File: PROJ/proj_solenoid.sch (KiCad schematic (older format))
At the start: 19 parts

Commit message: creating kicad project for PROJ
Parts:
- removed D?: RED_LED, symbol Device:LED
- removed D?: GREEN_LED, symbol Device:LED
- removed M?: Stepper_Motor_bipolar, symbol Motor:Stepper_Motor_bipolar
- removed R3, R4: 470, symbol Device:R
- removed SW? (x2): SW_Push, symbol Switch:SW_Push
- removed U?: L298HN, Package_TO_SOT_THT:TO-220-15_P2.54x2.54mm_StaggerOdd_Lead4.58mm_Vertical, symbol Driver_Motor:L298HN
- added D?: LED, symbol Device:LED
- added R?: 10k, symbol Device:R
- added SW?: SW_Reed, symbol Switch:SW_Reed
- added U?: 74HC595, symbol My_lib:74HC596
- added U?: analog_keypad, symbol My_lib:analog_keypad
- added U?: 74LS151, symbol 74xx:74LS151
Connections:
- net labels added: Keypad, Magnet_Mux, Magnet_Sensor, Mux_S0, Mux_S1, Mux_S2, Solenoid_CLK, Solenoid_DATA, Solenoid_RESET, Solenoid_STORE
- net labels removed: +12V, Button_User_1, Button_User_2, Green_LED, Motor_IN1, Motor_IN2, Motor_IN3, Motor_IN4, Red_LED
- wire segments 76 -> 82
- no-connect marks 5 -> 9
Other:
- note added: "Each partition will have its own magnet detector, \nwhich will detect if its open or not."
- note added: "Led signaling that partition is open"
- note added: "Multiplexer for connecting multiple sensors"
- note added: "Shift register used for operating solenoids"
- note added: "Solenoid used for locking individual partitions. \nOperated trough shift register."
- note removed: "External psu needed"
- note removed: "LED for potencial notifying user"
- note removed: "Solenoid can be used for locking mechanism.\nMultiple solenoids can be added using shift register."
- note removed: "Stepper motor could be used for mechanism which would allow circular\nmovement of pill partitions, allowing only one to be accest at a time.\nNot big fan of this approach."
- note removed: "Two user buttons \nOne can be used for canceling alarm\nSecond for entering time setup phase\n"
- moved on the sheet: R1, R2, R5

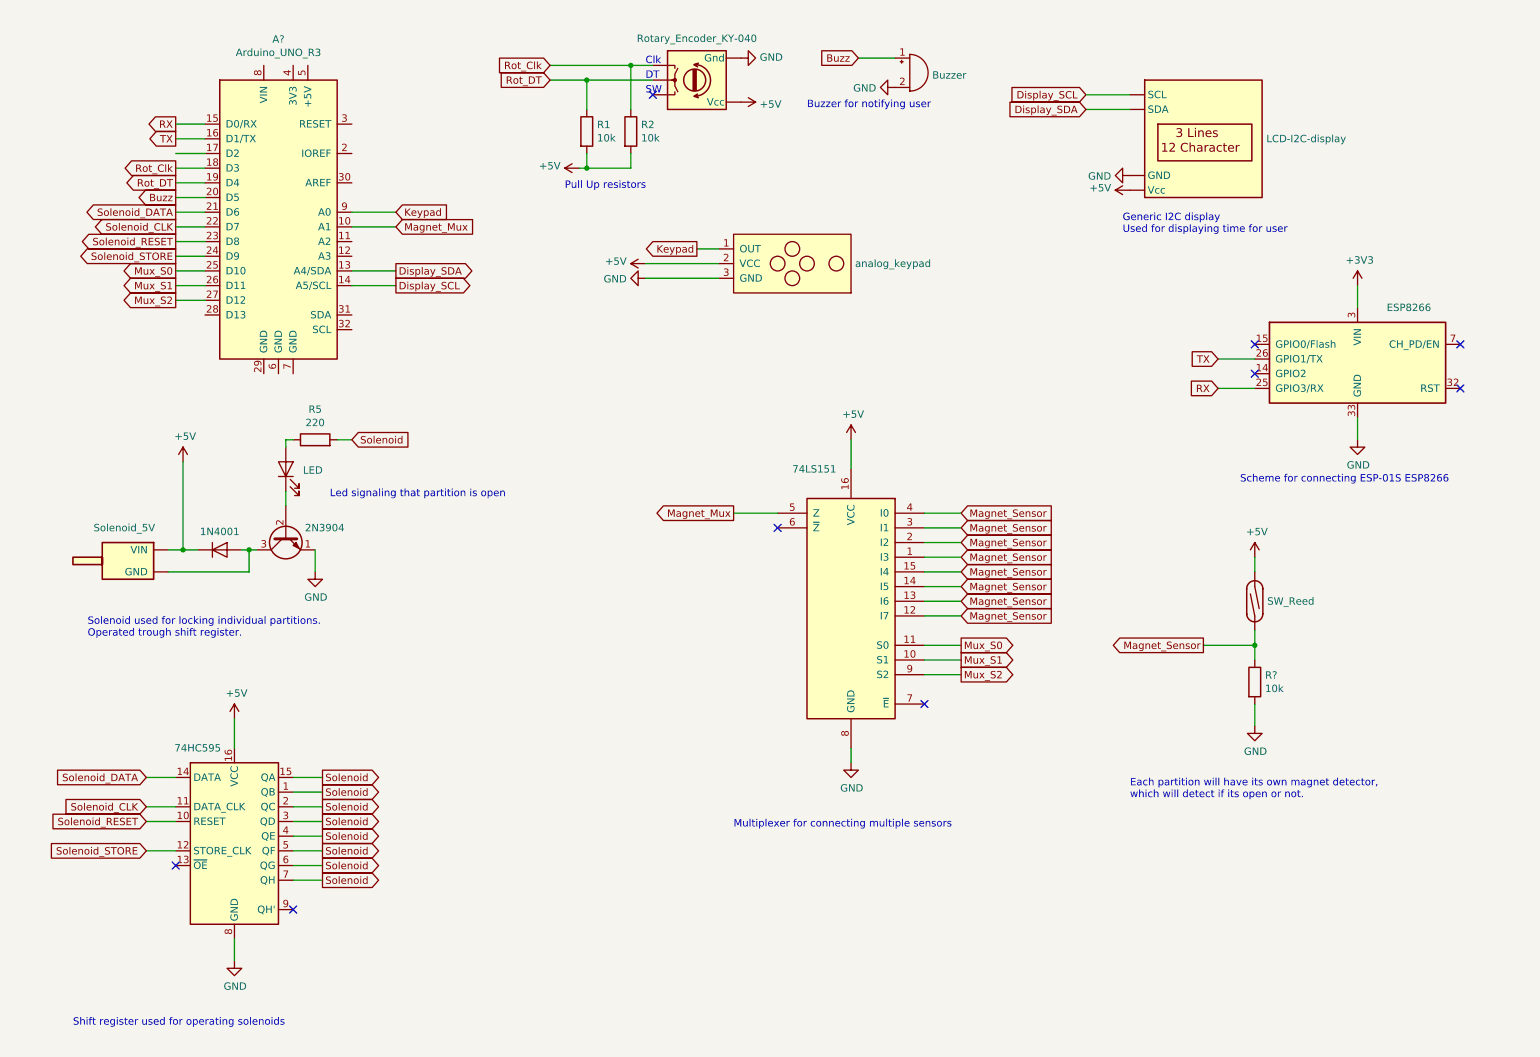
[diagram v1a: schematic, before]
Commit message: adding backup batery to proj
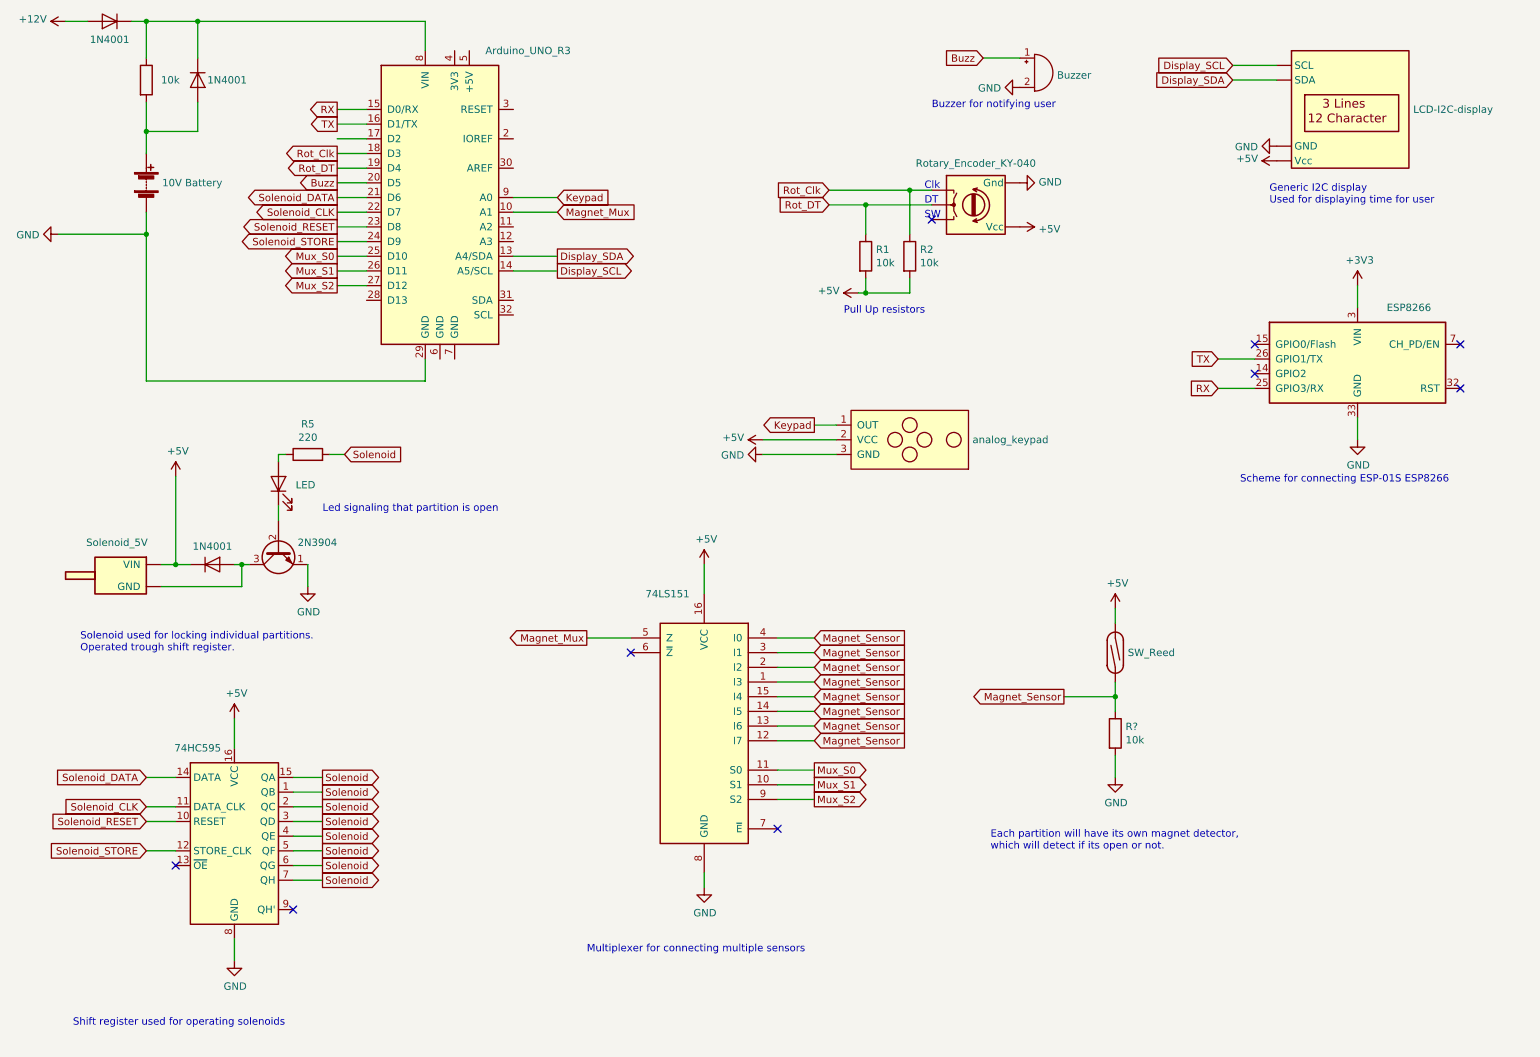
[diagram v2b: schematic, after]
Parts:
- added BT?: 10V Battery, symbol Device:Battery
- added D? (x2): 1N4001, Diode_THT:D_DO-41_SOD81_P10.16mm_Horizontal, symbol Diode:1N4001
- added R?: 10k, symbol Device:R
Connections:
- net GND: now also A?.29 (GND), BT?.2 (-)
- net at A?.8 (VIN): now also D?.1 (K), D?.1 (K), R?.1
- new net: BT?.1 (+), D?.2 (A), R?.2
- new net +12V: D?.2 (A)
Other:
- moved on the sheet: R1, R2, R5, R?

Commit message: projV1_4
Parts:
- removed BZ?: Buzzer, symbol Device:Buzzer
- added LS?: Speaker, symbol Device:Speaker
- added SW?: SW_DIP_x01, symbol Switch:SW_DIP_x01
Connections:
- net +3V3: now also SW?.2
- net Buzz: now also LS?.1; no longer A?.20 (D5)
- net GND: now also LS?.2
- net Offline-online_switch: now reaches A?.11 (A2)
- net Offline-online_switch: now also SW?.1
- new net Speaker: A?.20 (D5)
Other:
- note added: "Speaker for notifying user"
- note added: "Switch for switching between \noffline and online mode"
- note removed: "Buzzer for notifying user"
- moved on the sheet: R1, R2
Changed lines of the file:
@@
 encoding utf-8
 Sheet 1 1
-Title "Pill helper V1.3 (solenoid approach)"
+Title "Pill helper V1.4 (solenoid approach)"
 Date "2020-12-26"
-Rev "1.3"
+Rev "1.4"
 Comp "FEL CVUT"
 Comment1 "First potential implementation of Pill helper"
@@
 L Device:Rotary_Encoder_KY-040 SW?
 U 1 1 5FD97BB7
-P 7250 2000
-F 0 "SW?" H 7250 2375 50  0001 C CNN
-F 1 "Rotary_Encoder_KY-040" H 7250 2283 50  0000 C CNN
-F 2 "" H 7100 2160 50  0001 C CNN
-F 3 "~" H 7250 2260 50  0001 C CNN
-	1    7250 2000
-	1    0    0    -1
-$EndComp
-Text Notes 6900 1900 0    50   ~ 0
+P 7950 2150
+F 0 "SW?" H 7950 2525 50  0001 C CNN
+F 1 "Rotary_Encoder_KY-040" H 7950 2433 50  0000 C CNN
+F 2 "" H 7800 2310 50  0001 C CNN
+F 3 "~" H 7950 2410 50  0001 C CNN
+	1    7950 2150
+	1    0    0    -1
+$EndComp
+Text Notes 7600 2050 0    50   ~ 0
 Clk
-Text Notes 6900 2000 0    50   ~ 0
+Text Notes 7600 2150 0    50   ~ 0
 DT
-Text Notes 6900 2100 0    50   ~ 0
+Text Notes 7600 2250 0    50   ~ 0
 SW
 $Comp
 L power:GND #PWR?
 U 1 1 5FDA60FC
-P 7550 1850
-F 0 "#PWR?" H 7550 1600 50  0001 C CNN
-F 1 "GND" V 7555 1722 50  0000 R CNN
-F 2 "" H 7550 1850 50  0001 C CNN
-F 3 "" H 7550 1850 50  0001 C CNN
-	1    7550 1850
+P 8250 2000
+F 0 "#PWR?" H 8250 1750 50  0001 C CNN
+F 1 "GND" V 8255 1872 50  0000 R CNN
+F 2 "" H 8250 2000 50  0001 C CNN
+F 3 "" H 8250 2000 50  0001 C CNN
+	1    8250 2000
 	0    -1   -1   0
 $EndComp
@@
 L power:+5V #PWR?
 U 1 1 5FDA6182
-P 7550 2150
-F 0 "#PWR?" H 7550 2000 50  0001 C CNN
-F 1 "+5V" V 7565 2278 50  0000 L CNN
-F 2 "" H 7550 2150 50  0001 C CNN
-F 3 "" H 7550 2150 50  0001 C CNN
-	1    7550 2150
+P 8250 2300
+F 0 "#PWR?" H 8250 2150 50  0001 C CNN
+F 1 "+5V" V 8265 2428 50  0000 L CNN
+F 2 "" H 8250 2300 50  0001 C CNN
+F 3 "" H 8250 2300 50  0001 C CNN
+	1    8250 2300
 	0    1    1    0
 $EndComp
@@
 Wire Wire Line
 	2900 1750 3100 1750
-Text GLabel 6250 1900 0    50   Input ~ 0
+Text GLabel 6950 2050 0    50   Input ~ 0
 Rot_Clk
-Text GLabel 6250 2000 0    50   Input ~ 0
+Text GLabel 6950 2150 0    50   Input ~ 0
 Rot_DT
 $Comp
 L power:+5V #PWR?
 U 1 1 5FDA62C3
-P 6450 2600
-F 0 "#PWR?" H 6450 2450 50  0001 C CNN
-F 1 "+5V" V 6465 2728 50  0000 L CNN
-F 2 "" H 6450 2600 50  0001 C CNN
-F 3 "" H 6450 2600 50  0001 C CNN
-	1    6450 2600
+P 7150 2750
+F 0 "#PWR?" H 7150 2600 50  0001 C CNN
+F 1 "+5V" V 7165 2878 50  0000 L CNN
+F 2 "" H 7150 2750 50  0001 C CNN
+F 3 "" H 7150 2750 50  0001 C CNN
+	1    7150 2750
 	0    -1   -1   0
 $EndComp
@@
 L Device:R R1
 U 1 1 5FDA6344
-P 6500 2350
-F 0 "R1" H 6570 2396 50  0000 L CNN
-F 1 "10k" H 6570 2305 50  0000 L CNN
-F 2 "" V 6430 2350 50  0001 C CNN
-F 3 "~" H 6500 2350 50  0001 C CNN
-	1    6500 2350
+P 7200 2500
+F 0 "R1" H 7270 2546 50  0000 L CNN
+F 1 "10k" H 7270 2455 50  0000 L CNN
+F 2 "" V 7130 2500 50  0001 C CNN
+F 3 "~" H 7200 2500 50  0001 C CNN
+	1    7200 2500
 	1    0    0    -1
 $EndComp
@@
 L Device:R R2
 U 1 1 5FDA63AE
-P 6800 2350
-F 0 "R2" H 6870 2396 50  0000 L CNN
-F 1 "10k" H 6870 2305 50  0000 L CNN
-F 2 "" V 6730 2350 50  0001 C CNN
-F 3 "~" H 6800 2350 50  0001 C CNN
-	1    6800 2350
-	1    0    0    -1
-$EndComp
-Wire Wire Line
-	6250 1900 6800 1900
-Wire Wire Line
-	6250 2000 6500 2000
-Wire Wire Line
-	6500 2200 6500 2000
-Connection ~ 6500 2000
-Wire Wire Line
-	6500 2000 6950 2000
-Wire Wire Line
-	6800 1900 6800 2200
-Connection ~ 6800 1900
-Wire Wire Line
-	6800 1900 6950 1900
-Wire Wire Line
-	6450 2600 6500 2600
-Wire Wire Line
-	6500 2600 6500 2500
-Wire Wire Line
-	6500 2600 6800 2600
-Wire Wire Line
-	6800 2600 6800 2500
-Connection ~ 6500 2600
-Text Notes 6350 2750 0    50   ~ 0
+P 7500 2500
+F 0 "R2" H 7570 2546 50  0000 L CNN
+F 1 "10k" H 7570 2455 50  0000 L CNN
+F 2 "" V 7430 2500 50  0001 C CNN
+F 3 "~" H 7500 2500 50  0001 C CNN
+	1    7500 2500
+	1    0    0    -1
+$EndComp
+Wire Wire Line
+	6950 2050 7500 2050
+Wire Wire Line
+	6950 2150 7200 2150
+Wire Wire Line
+	7200 2350 7200 2150
+Connection ~ 7200 2150
+Wire Wire Line
+	7200 2150 7650 2150
+Wire Wire Line
+	7500 2050 7500 2350
+Connection ~ 7500 2050
+Wire Wire Line
+	7500 2050 7650 2050
+Wire Wire Line
+	7150 2750 7200 2750
+Wire Wire Line
+	7200 2750 7200 2650
+Wire Wire Line
+	7200 2750 7500 2750
+Wire Wire Line
+	7500 2750 7500 2650
+Connection ~ 7200 2750
+Text Notes 7050 2900 0    50   ~ 0
 Pull Up resistors
 Text GLabel 2900 1850 0    50   Output ~ 0
-Buzz
-$Comp
-L Device:Buzzer BZ?
-U 1 1 5FDA69A7
-P 7650 1100
-F 0 "BZ?" H 7803 1129 50  0001 L CNN
-F 1 "Buzzer" H 7803 1083 50  0000 L CNN
-F 2 "" V 7625 1200 50  0001 C CNN
-F 3 "~" V 7625 1200 50  0001 C CNN
-	1    7650 1100
-	1    0    0    -1
-$EndComp
+Speaker
 Text GLabel 7300 1000 0    50   Input ~ 0
 Buzz
@@
 L power:GND #PWR?
 U 1 1 5FDA6EF6
-P 7550 1200
-F 0 "#PWR?" H 7550 950 50  0001 C CNN
-F 1 "GND" V 7555 1072 50  0000 R CNN
-F 2 "" H 7550 1200 50  0001 C CNN
-F 3 "" H 7550 1200 50  0001 C CNN
-	1    7550 1200
+P 7500 1100
+F 0 "#PWR?" H 7500 850 50  0001 C CNN
+F 1 "GND" V 7505 972 50  0000 R CNN
+F 2 "" H 7500 1100 50  0001 C CNN
+F 3 "" H 7500 1100 50  0001 C CNN
+	1    7500 1100
 	0    1    1    0
 $EndComp
@@
 Wire Wire Line
 	2900 2450 3100 2450
-Text Notes 6950 1350 0    50   ~ 0
-Buzzer for notifying user
+Text Notes 7150 1350 0    50   ~ 0
+Speaker for notifying user
 $Comp
 L Display_Character:EA_T123X-I2C U?
@@
 Wire Wire Line
 	3100 2350 2900 2350
-NoConn ~ 6950 2100
+NoConn ~ 7650 2250
 Wire Wire Line
 	2700 4450 2700 4600
@@
 L My_lib:analog_keypad U?
 U 1 1 5FEF2A01
-P 6800 3600
-F 0 "U?" H 6800 3800 50  0001 C CNN
-F 1 "analog_keypad" H 7227 3600 50  0000 L CNN
-F 2 "" H 6800 3800 50  0001 C CNN
-F 3 "" H 6800 3800 50  0001 C CNN
-	1    6800 3600
+P 7500 3650
+F 0 "U?" H 7500 3850 50  0001 C CNN
+F 1 "analog_keypad" H 7927 3650 50  0000 L CNN
+F 2 "" H 7500 3850 50  0001 C CNN
+F 3 "" H 7500 3850 50  0001 C CNN
+	1    7500 3650
 	1    0    0    -1
 $EndComp
@@
 Wire Wire Line
 	4100 1950 4400 1950
-Text GLabel 6150 3500 0    50   Output ~ 0
+Text GLabel 6850 3550 0    50   Output ~ 0
 Keypad
 $Comp
 L power:+5V #PWR?
 U 1 1 5FEF769C
-P 5800 3600
-F 0 "#PWR?" H 5800 3450 50  0001 C CNN
-F 1 "+5V" V 5815 3728 50  0000 L CNN
-F 2 "" H 5800 3600 50  0001 C CNN
-F 3 "" H 5800 3600 50  0001 C CNN
-	1    5800 3600
+P 6500 3650
+F 0 "#PWR?" H 6500 3500 50  0001 C CNN
+F 1 "+5V" V 6515 3778 50  0000 L CNN
+F 2 "" H 6500 3650 50  0001 C CNN
+F 3 "" H 6500 3650 50  0001 C CNN
+	1    6500 3650
 	0    -1   -1   0
 $EndComp
 Wire Wire Line
-	6300 3500 6150 3500
-Wire Wire Line
-	6300 3600 5800 3600
+	7000 3550 6850 3550
+Wire Wire Line
+	7000 3650 6500 3650
 $Comp
 L power:GND #PWR?
 U 1 1 5FEF9D8F
-P 5800 3700
-F 0 "#PWR?" H 5800 3450 50  0001 C CNN
-F 1 "GND" V 5805 3572 50  0000 R CNN
-F 2 "" H 5800 3700 50  0001 C CNN
-F 3 "" H 5800 3700 50  0001 C CNN
-	1    5800 3700
+P 6500 3750
+F 0 "#PWR?" H 6500 3500 50  0001 C CNN
+F 1 "GND" V 6505 3622 50  0000 R CNN
+F 2 "" H 6500 3750 50  0001 C CNN
+F 3 "" H 6500 3750 50  0001 C CNN
+	1    6500 3750
 	0    1    1    0
 $EndComp
 Wire Wire Line
-	6300 3700 5800 3700
+	7000 3750 6500 3750
 $Comp
 L 74xx:74LS151 U?
@@
 	0    1    1    0
 $EndComp
+$Comp
+L Device:Speaker LS?
+U 1 1 60008504
+P 7750 1000
+F 0 "LS?" H 7920 996 50  0001 L CNN
+F 1 "Speaker" H 7920 950 50  0000 L CNN
+F 2 "" H 7750 800 50  0001 C CNN
+F 3 "~" H 7740 950 50  0001 C CNN
+	1    7750 1000
+	1    0    0    -1
+$EndComp
+Wire Wire Line
+	7550 1100 7500 1100
+Text GLabel 4400 2150 2    50   Input ~ 0
+Offline-online_switch
+Wire Wire Line
+	4100 2150 4400 2150
+$Comp
+L Switch:SW_DIP_x01 SW?
+U 1 1 60016750
+P 5950 1100
+F 0 "SW?" H 5950 1367 50  0001 C CNN
+F 1 "SW_DIP_x01" H 5950 1275 50  0000 C CNN
+F 2 "" H 5950 1100 50  0001 C CNN
+F 3 "" H 5950 1100 50  0001 C CNN
+	1    5950 1100
+	1    0    0    -1
+$EndComp
+Text GLabel 5550 1100 0    50   Output ~ 0
+Offline-online_switch
+$Comp
+L power:+3.3V #PWR?
+U 1 1 6001D755
+P 6450 1100
+F 0 "#PWR?" H 6450 950 50  0001 C CNN
+F 1 "+3.3V" V 6465 1228 50  0000 L CNN
+F 2 "" H 6450 1100 50  0001 C CNN
+F 3 "" H 6450 1100 50  0001 C CNN
+	1    6450 1100
+	0    1    1    0
+$EndComp
+Wire Wire Line
+	6450 1100 6250 1100
+Wire Wire Line
+	5650 1100 5550 1100
+Text Notes 5350 1400 0    50   ~ 0
+Switch for switching between \noffline and online mode
 $EndSCHEMATC

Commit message: I wanna die
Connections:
- net Buzz is gone; now on net Speaker: LS?.1
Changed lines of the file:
@@
 Speaker
 Text GLabel 7300 1000 0    50   Input ~ 0
-Buzz
+Speaker
 Wire Wire Line
 	7300 1000 7550 1000
